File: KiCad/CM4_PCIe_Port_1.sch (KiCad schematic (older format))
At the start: 1 part, among them J13 10018783-10113TLF

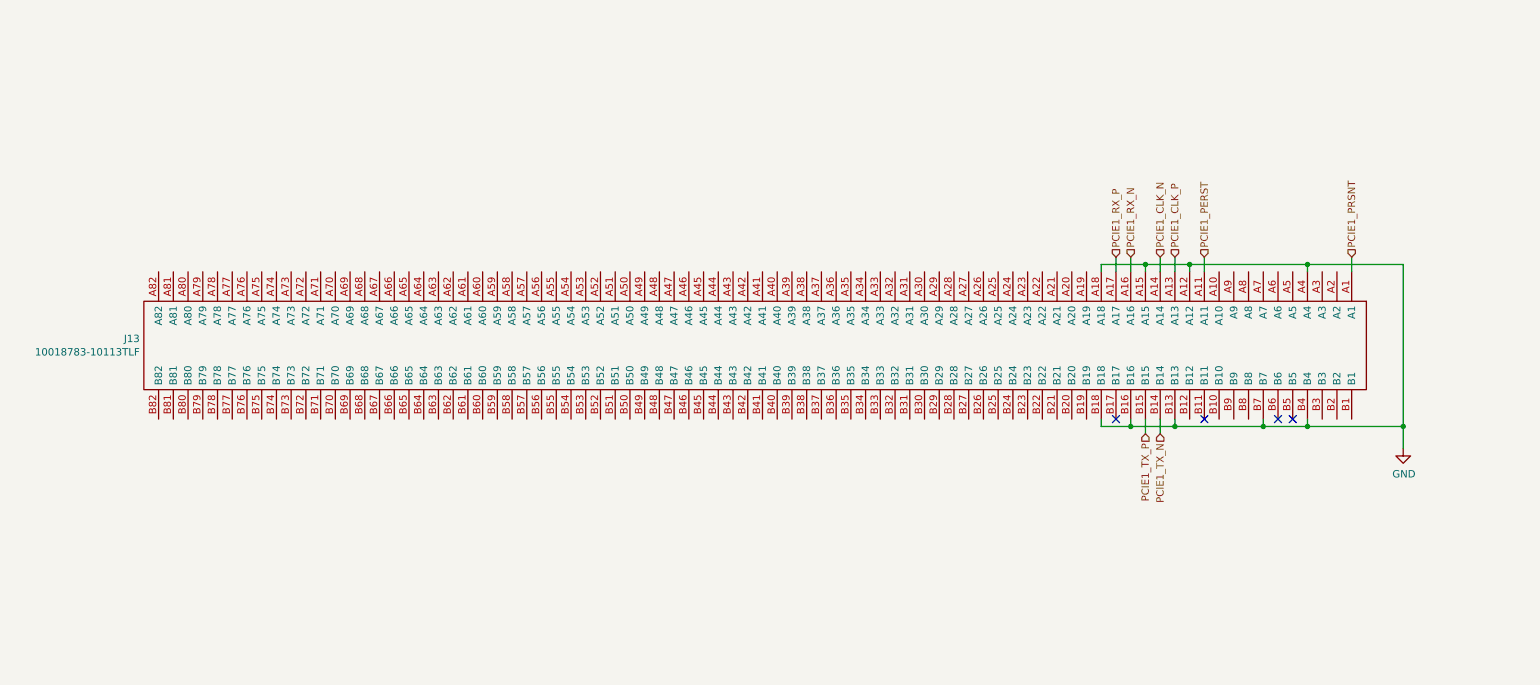
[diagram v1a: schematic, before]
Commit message: Updating PCIe symbols + PCIe power stub sheet
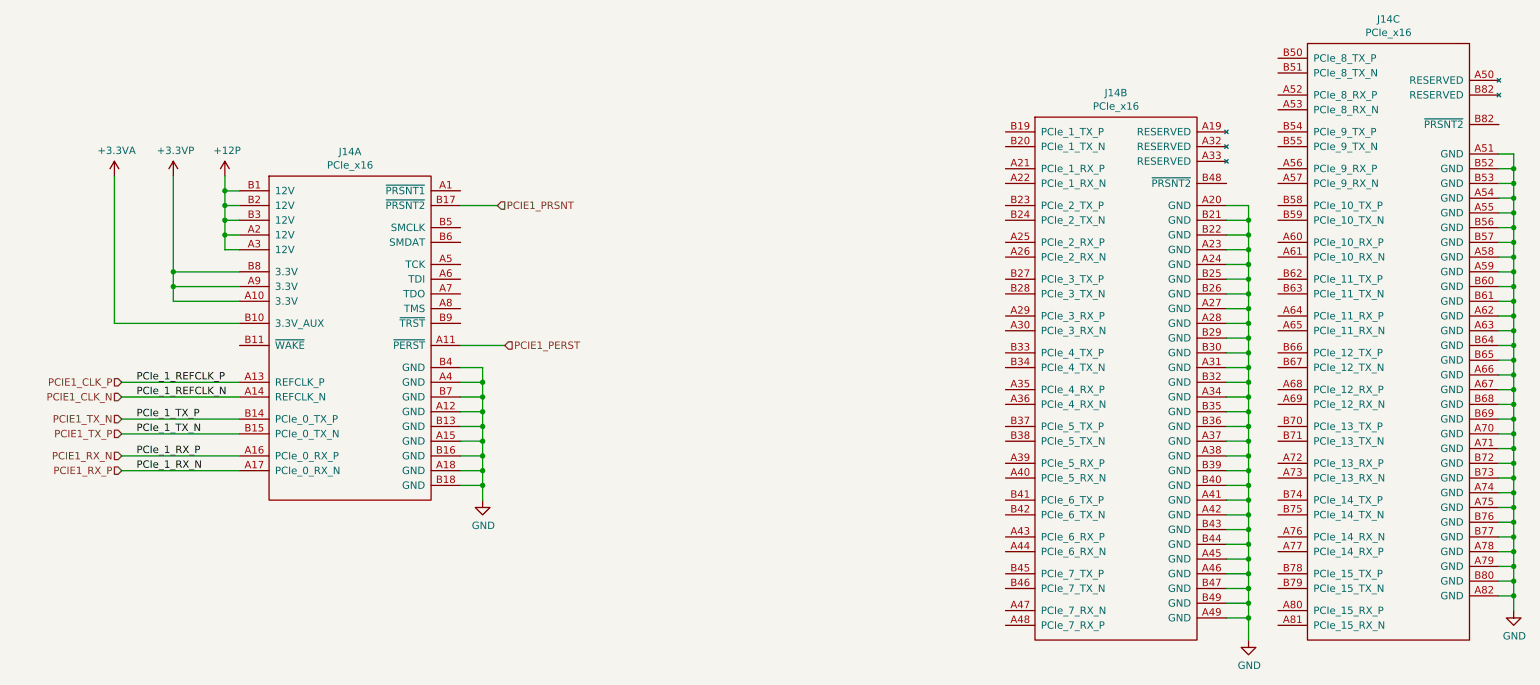
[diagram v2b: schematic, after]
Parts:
- removed J13: 10018783-10113TLF, 10018783-10113TLF, symbol CM4_MATX:10018783-10113TLF
- added J14: PCIe_x16, CM4_MATX:10018783-10113TLF, symbol CM4_MATX:PCIe_x16
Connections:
- net GND: now also J14.A12 (GND), J14.A15 (GND), J14.A18 (GND), J14.A20 (GND), J14.A23 (GND), J14.A24 (GND), J14.A27 (GND), J14.A28 (GND), J14.A31 (GND), J14.A34 (GND), J14.A37 (GND), J14.A38 (GND), J14.A4 (GND), J14.A41 (GND), J14.A42 (GND), J14.A45 (GND), J14.A46 (GND), J14.A49 (GND), J14.A51 (GND), J14.A54 (GND), J14.A55 (GND), J14.A58 (GND), J14.A59 (GND), J14.A62 (GND), J14.A63 (GND), J14.A66 (GND), J14.A67 (GND), J14.A70 (GND), J14.A71 (GND), J14.A74 (GND), J14.A75 (GND), J14.A78 (GND), J14.A79 (GND), J14.A82 (GND), J14.B13 (GND), J14.B16 (GND), J14.B18 (GND), J14.B21 (GND), J14.B22 (GND), J14.B25 (GND), J14.B26 (GND), J14.B29 (GND), J14.B30 (GND), J14.B32 (GND), J14.B35 (GND), J14.B36 (GND), J14.B39 (GND), J14.B4 (GND), J14.B40 (GND), J14.B43 (GND), J14.B44 (GND), J14.B47 (GND), J14.B49 (GND), J14.B52 (GND), J14.B53 (GND), J14.B56 (GND), J14.B57 (GND), J14.B60 (GND), J14.B61 (GND), J14.B64 (GND), J14.B65 (GND), J14.B68 (GND), J14.B69 (GND), J14.B7 (GND), J14.B72 (GND), J14.B73 (GND), J14.B76 (GND), J14.B77 (GND), J14.B80 (GND)
- net PCIE1_CLK_N: now also J14.A14 (REFCLK_N)
- net PCIE1_CLK_P: now also J14.A13 (REFCLK_P)
- net PCIE1_PERST: now also J14.A11 (~PERST)
- net PCIE1_PRSNT: now also J14.B17 (~PRSNT2)
- net PCIE1_RX_N: now also J14.A16 (PCIe_0_RX_P)
- net PCIE1_RX_P: now also J14.A17 (PCIe_0_RX_N)
- net PCIE1_TX_N: now also J14.B14 (PCIe_0_TX_P)
- net PCIE1_TX_P: now also J14.B15 (PCIe_0_TX_N)
- new net +12P: J14.A2 (12V), J14.A3 (12V), J14.B1 (12V), J14.B2 (12V), J14.B3 (12V)
- new net +3.3VA: J14.B10 (3.3V_AUX)
- new net +3.3VP: J14.A10 (3.3V), J14.A9 (3.3V), J14.B8 (3.3V)
- no-connect marks 4 -> 0
